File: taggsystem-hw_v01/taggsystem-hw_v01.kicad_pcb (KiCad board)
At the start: 2 copper layers, 107 x 82 mm, 1 part, among them U1 ESP32-DevKitC-32E

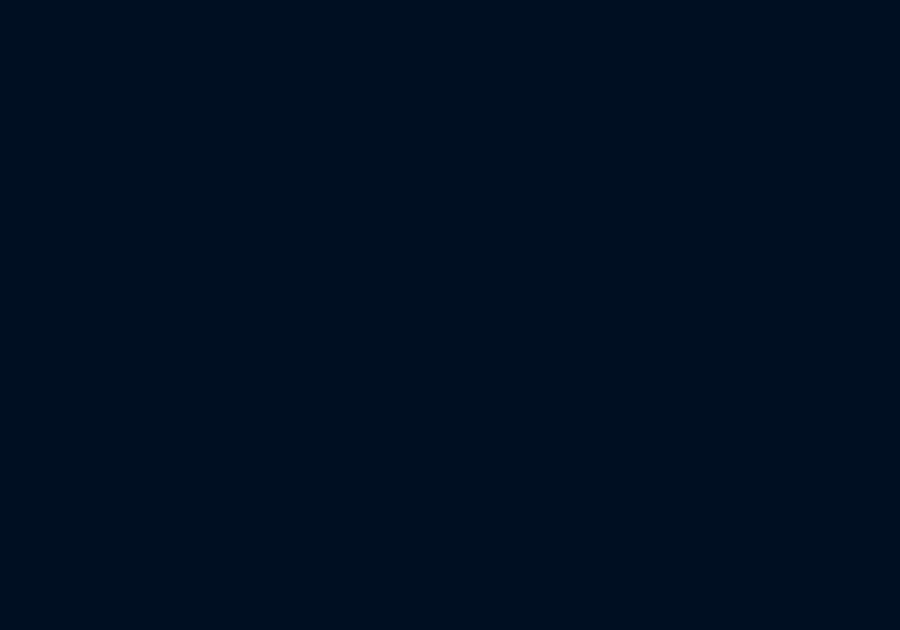
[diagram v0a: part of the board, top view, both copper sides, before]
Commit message: Add part number and manifacturer
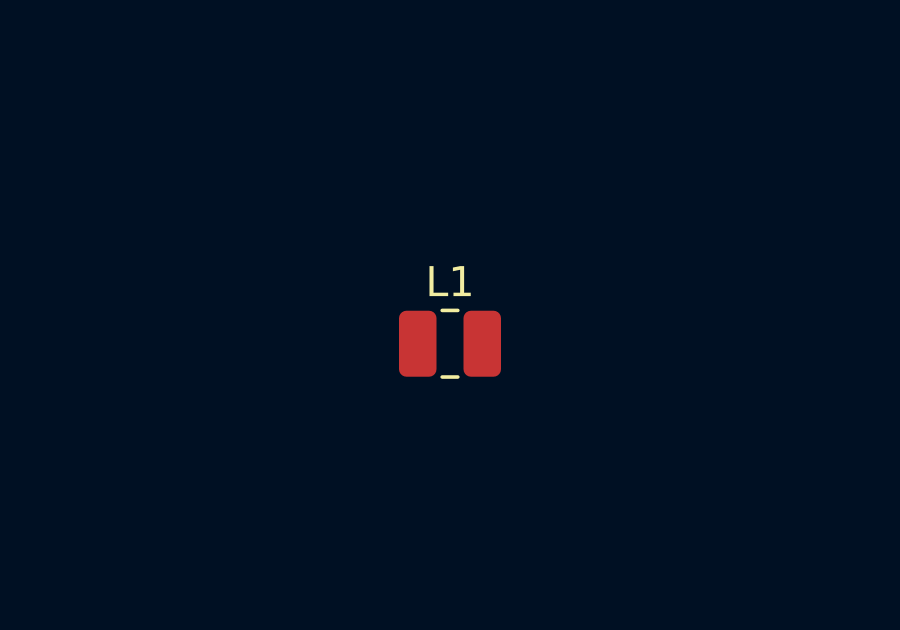
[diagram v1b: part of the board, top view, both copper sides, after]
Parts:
- added L1: ~, taggsystem_library:L_1008_2520Metric, F.Cu at (197.0, 70.5)
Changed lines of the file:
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@@
   (net 37 "unconnected-(U1-5V-Pad19A)")
   (net 38 "unconnected-(U1-CLK-Pad19B)")
+  (net 39 "unconnected-(L1-Pad1)")
+  (net 40 "unconnected-(L1-Pad2)")
+  (footprint "taggsystem_library:L_1008_2520Metric" (layer "F.Cu")
+    (at 197.045 70.485)
+    (descr "Inductor SMD 1008 (2520 Metric), square (rectangular) end terminal, IPC_7351 nominal, (Body size source: https://ecsxtal.com/store/pdf/ECS-MPI2520-SMD-POWER-INDUCTOR.pdf), generated with kicad-footprint-generator")
+    (tags "inductor")
+    (property "Sheetfile" "taggsystem-hw_v01.kicad_sch")
+    (property "Sheetname" "")
+    (attr smd)
+    (fp_text reference "L1" (at 0 -2.05) (layer "F.SilkS")
+        (effects (font (size 1 1) (thickness 0.15)))
+    )
+    (fp_text value "~" (at 0 2.05) (layer "F.Fab")
+        (effects (font (size 1 1) (thickness 0.15)))
+    )
+    (fp_text user "${REFERENCE}" (at 0 0) (layer "F.Fab")
+        (effects (font (size 0.62 0.62) (thickness 0.09)))
+    )
+    (fp_line (start -0.261252 -1.11) (end 0.261252 -1.11)
+      (stroke (width 0.12) (type solid)) (layer "F.SilkS"))
+    (fp_line (start -0.261252 1.11) (end 0.261252 1.11)
+      (stroke (width 0.12) (type solid)) (layer "F.SilkS"))
+    (fp_line (start -1.95 -1.35) (end 1.95 -1.35)
+      (stroke (width 0.05) (type solid)) (layer "F.CrtYd"))
+    (fp_line (start -1.95 1.35) (end -1.95 -1.35)
+      (stroke (width 0.05) (type solid)) (layer "F.CrtYd"))
+    (fp_line (start 1.95 -1.35) (end 1.95 1.35)
+      (stroke (width 0.05) (type solid)) (layer "F.CrtYd"))
+    (fp_line (start 1.95 1.35) (end -1.95 1.35)
+      (stroke (width 0.05) (type solid)) (layer "F.CrtYd"))
+    (fp_line (start -1.25 -1) (end 1.25 -1)
+      (stroke (width 0.1) (type solid)) (layer "F.Fab"))
+    (fp_line (start -1.25 1) (end -1.25 -1)
+      (stroke (width 0.1) (type solid)) (layer "F.Fab"))
+    (fp_line (start 1.25 -1) (end 1.25 1)
+      (stroke (width 0.1) (type solid)) (layer "F.Fab"))
+    (fp_line (start 1.25 1) (end -1.25 1)
+      (stroke (width 0.1) (type solid)) (layer "F.Fab"))
+    (pad "1" smd roundrect (at -1.075 0) (size 1.25 2.2) (layers "F.Cu" "F.Paste" "F.Mask") (roundrect_rratio 0.2)
+      (net 39 "unconnected-(L1-Pad1)") (pinfunction "1") (pintype "passive"))
+    (pad "2" smd roundrect (at 1.075 0) (size 1.25 2.2) (layers "F.Cu" "F.Paste" "F.Mask") (roundrect_rratio 0.2)
+      (net 40 "unconnected-(L1-Pad2)") (pinfunction "2") (pintype "passive"))
+    (model "${KICAD6_3DMODEL_DIR}/Inductor_SMD.3dshapes/L_1008_2520Metric.wrl"
+      (offset (xyz 0 0 0))
+      (scale (xyz 1 1 1))
+      (rotate (xyz 0 0 0))
+    )
+  )
   (footprint "taggsystem_library:ESP32-DEVKITC32E" (layer "F.Cu")
     (at 144.6 76.28)

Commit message: Add to KiCad project
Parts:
- added U2: ~, 00_SOT:SOT23-6, F.Cu at (183.4, 58.1)
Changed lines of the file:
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@@
   (net 39 "unconnected-(L1-Pad1)")
   (net 40 "unconnected-(L1-Pad2)")
+  (net 41 "unconnected-(U2-GND-Pad1)")
+  (net 42 "unconnected-(U2-SW-Pad2)")
+  (net 43 "unconnected-(U2-VIN-Pad3)")
+  (net 44 "unconnected-(U2-VFB-Pad4)")
+  (net 45 "unconnected-(U2-EN-Pad5)")
+  (net 46 "unconnected-(U2-BST-Pad6)")
+  (footprint "00_SOT:SOT23-6" (layer "F.Cu")
+    (at 183.435 58.105)
+    (property "Mfg1" "TI")
+    (property "Mfg1 pn" "TPS561201DDCR")
+    (property "Sheetfile" "taggsystem-hw_v01.kicad_sch")
+    (property "Sheetname" "")
+    (attr smd)
+    (fp_text reference "U2" (at 0.5 -2.1 unlocked) (layer "F.SilkS")
+        (effects (font (size 1 1) (thickness 0.1)))
+    )
+    (fp_text value "~" (at 0.1 2.7 unlocked) (layer "F.Fab")
+        (effects (font (size 1 1) (thickness 0.15)))
+    )
+    (fp_text user "${REFERENCE}" (at 0 4.3 unlocked) (layer "F.Fab")
+        (effects (font (size 1 1) (thickness 0.15)))
+    )
+    (fp_rect (start -0.75 -1.25) (end 0.75 1.25)
+      (stroke (width 0.1) (type default)) (fill none) (layer "F.Fab"))
+    (fp_circle (center -0.4 -0.9) (end -0.4 -0.7)
+      (stroke (width 0.1) (type default)) (fill none) (layer "F.Fab"))
+    (pad "1" smd roundrect (at -1.35 -0.95) (size 1.1 0.6) (layers "F.Cu" "F.Paste" "F.Mask") (roundrect_rratio 0.25)
+      (net 41 "unconnected-(U2-GND-Pad1)") (pinfunction "GND") (pintype "input") (thermal_bridge_angle 45))
+    (pad "2" smd roundrect (at -1.35 0) (size 1.1 0.6) (layers "F.Cu" "F.Paste" "F.Mask") (roundrect_rratio 0.25)
+      (net 42 "unconnected-(U2-SW-Pad2)") (pinfunction "SW") (pintype "input") (thermal_bridge_angle 45))
+    (pad "3" smd roundrect (at -1.35 0.95) (size 1.1 0.6) (layers "F.Cu" "F.Paste" "F.Mask") (roundrect_rratio 0.25)
+      (net 43 "unconnected-(U2-VIN-Pad3)") (pinfunction "VIN") (pintype "input") (thermal_bridge_angle 45))
+    (pad "4" smd roundrect (at 1.35 0.95) (size 1.1 0.6) (layers "F.Cu" "F.Paste" "F.Mask") (roundrect_rratio 0.25)
+      (net 44 "unconnected-(U2-VFB-Pad4)") (pinfunction "VFB") (pintype "input") (thermal_bridge_angle 45))
+    (pad "5" smd roundrect (at 1.35 0) (size 1.1 0.6) (layers "F.Cu" "F.Paste" "F.Mask") (roundrect_rratio 0.25)
+      (net 45 "unconnected-(U2-EN-Pad5)") (pinfunction "EN") (pintype "input") (thermal_bridge_angle 45))
+    (pad "6" smd roundrect (at 1.35 -0.95) (size 1.1 0.6) (layers "F.Cu" "F.Paste" "F.Mask") (roundrect_rratio 0.25)
+      (net 46 "unconnected-(U2-BST-Pad6)") (pinfunction "BST") (pintype "input") (thermal_bridge_angle 45))
+  )
   (footprint "taggsystem_library:L_1008_2520Metric" (layer "F.Cu")
     (at 197.045 70.485)
